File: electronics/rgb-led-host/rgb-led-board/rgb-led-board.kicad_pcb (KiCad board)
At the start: 2 copper layers, 13 parts, among them P1 PAD_SOLDER_5mm, P2 PAD_SOLDER_5mm, P3 CONN_01X06, P4 PAD_SOLDER_5mm, P5 PAD_SOLDER_5mm, P6 PAD_SOLDER_5mm, P7 PAD_SOLDER_5mm, U1 AL1793AFE-13

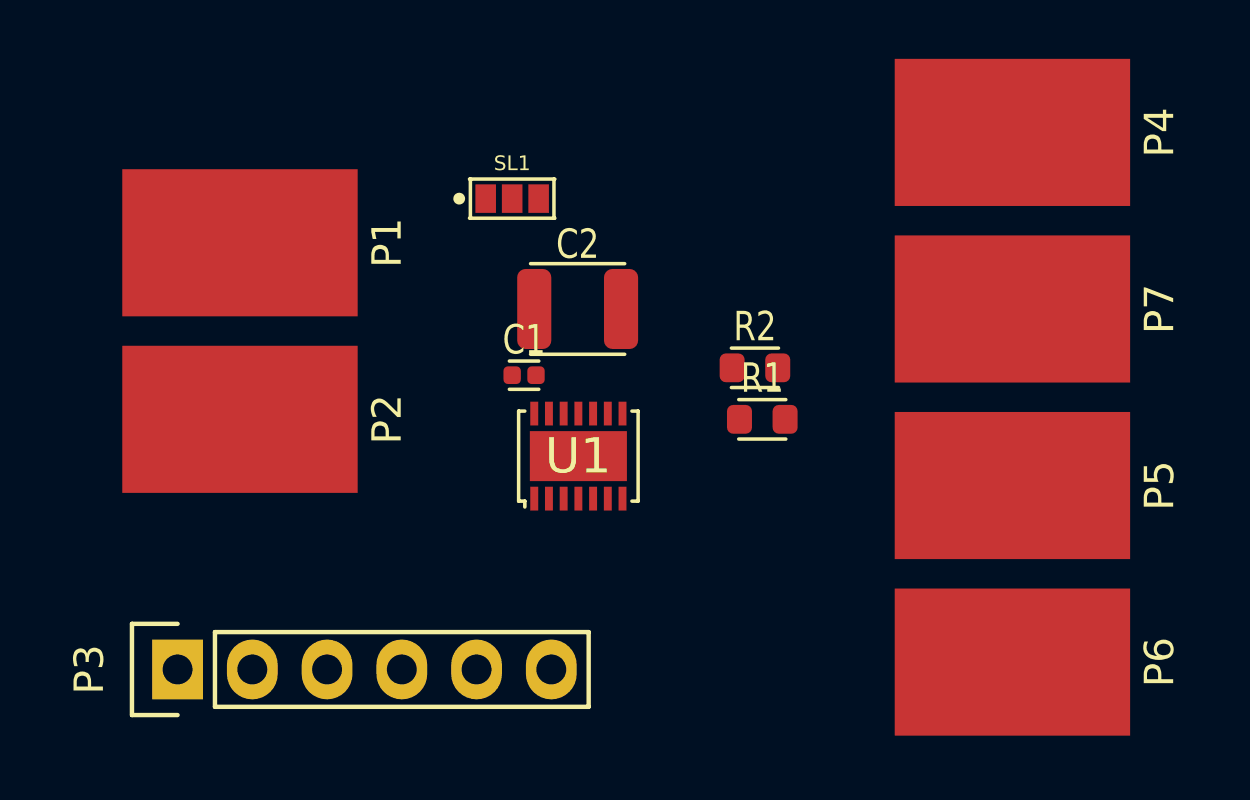
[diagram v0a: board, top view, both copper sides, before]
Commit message: Updates to schematic and PCB layout
Routed and cosmetics placed.
Ready for fab exports.
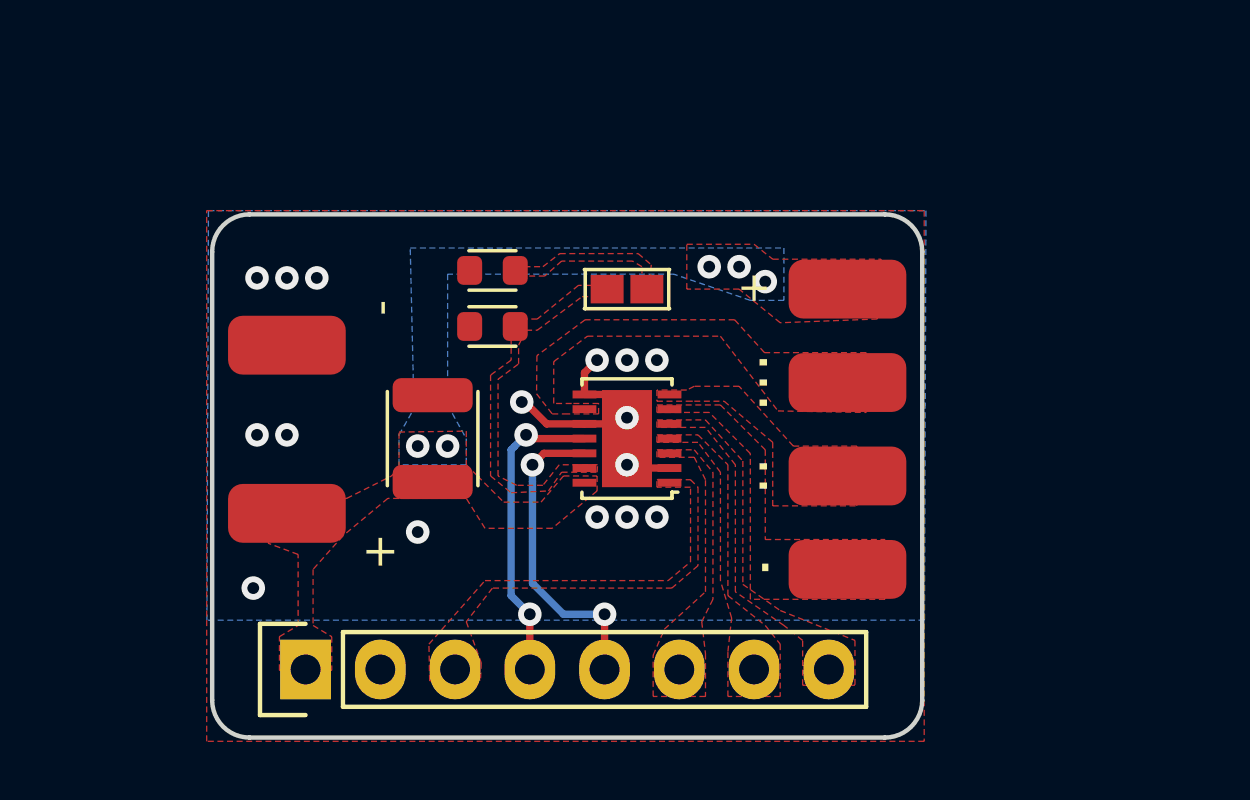
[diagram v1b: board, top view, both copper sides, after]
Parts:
- removed C2: 22u_X7R_3225M, Applidyne_Capacitor:CAPC3225X170N
- C1: value 100n_X7R_1005M -> 22u_X7R_3225M; footprint Applidyne_Capacitor:CAPC1005X60N -> Applidyne_Capacitor:CAPC3225X170N
- P1, P2, P4, P5, P6, P7: value PAD_SOLDER_5mm -> PAD_SOLDER_2mm; footprint Applidyne_Connector:PAD_SOLDER_5mm -> Applidyne_Connector:PAD_SOLDER_2mm
- P3: value CONN_01X06 -> CONN_01X08; footprint Applidyne_Connector_Wurth:61300611121 -> Applidyne_Connector_Wurth:61300811121
- SL1: value SOLDER-LINK-3 -> SOLDER-LINK-2; footprint Applidyne_Link:SJ1608-3N -> Applidyne_Link:SJ1608-2N
- moved R1 10.5 mm to (132.1, 59.7), turned to 180 degrees
- moved P1 9.33 mm to (125.1, 67.9)
- moved R2 9.03 mm to (132.1, 61.6), turned to 180 degrees
- moved P6 8.45 mm to (144.1, 66.7)
- moved P4 7.73 mm to (144.1, 60.3)
- moved P5 6.29 mm to (144.1, 69.8)
- moved P7 6.14 mm to (144.1, 63.5)
- moved SL1 4.97 mm to (136.7, 60.3), turned to 180 degrees
- moved P3 4.35 mm to (125.7, 73.2)
- moved C1 3.78 mm to (130.0, 65.4), turned to 90 degrees
- moved P2 2.98 mm to (125.1, 62.2)
- moved U1 1.76 mm to (136.7, 65.4), turned to 90 degrees
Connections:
- C1 pad 1: GND -> +POWER
- C1 pad 2: +POWER -> GND
- P3 pad 1: /ENABLE -> +POWER
- P3 pad 2: /FAULT -> GND
- P3 pad 3: /POWER_GOOD -> /ENABLE
- P3 pad 4: /PWM1 -> /POWER_GOOD
- P3 pad 5: /PWM2 -> /~FAULT
- SL1 pad 2: Net-(SL1-Pad2) -> Net-(R2-Pad1)
- U1 pad 12: /FAULT -> /~FAULT
- U1 pad 13: Net-(SL1-Pad2) -> Net-(R2-Pad1)
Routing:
- net /~FAULT: track 0.00 -> 10.7 mm, vias 0 -> 2
- net /POWER_GOOD: track 0.00 -> 10.5 mm, vias 0 -> 2
- net GND: track 0.00 -> 8.75 mm, vias 0 -> 16
- net /LED_2: track 0.00 -> 1.02 mm
- net +POWER: vias 0 -> 5
- added copper zone on B.Cu, net +POWER
- added copper zone on F.Cu, net +POWER
- added copper zone on F.Cu, net /ENABLE
- added copper zone on F.Cu, net /LED_1
- added copper zone on F.Cu, net /LED_2
- added copper zone on F.Cu, net /LED_3
- added copper zone on F.Cu, net /PWM1
- added copper zone on F.Cu, net /PWM2
- added copper zone on F.Cu, net /PWM3
- added copper zone on B.Cu, net GND
- added copper zone on F.Cu, net GND
- added copper zone on F.Cu, net Net-(R1-Pad1)
- added copper zone on F.Cu, net Net-(R2-Pad1)
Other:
- board outline added: 24.1 x 17.8 mm
- board text added: "+"
- board text added: "-"
- board text added: "."
- board text added: ".."
- board text added: "1"
- board text added: "2"
- board text added: "2018 S.Rapson"
- board text added: "3"
- board text added: "EN"
- board text added: "GND"
- board text added: "PG"
- board text added: "VCC"
- board text added: "max 30V"
- board text added: "~FAULT"
- board text added: "…"
